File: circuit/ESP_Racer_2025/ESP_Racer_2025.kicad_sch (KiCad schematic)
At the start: 19 parts, among them IC1 XCL102D333CR-G, J1 Conn_LED_1, J2 Conn_LED_2, J3 Conn_Servo, U1 DRV8835DSST, U2 SFV12R-2STE1LF, U3 ESP32-C3-WROOM-02

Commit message: pcb fix
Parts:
- J1, J2: footprint JST_ZH_B2B-ZR_1x02_P1.50mm_Vertical:JST_ZH_B2B-ZR_1x02_P1.50mm_Vertical -> Molex:Molex_PicoBlade_53047-0210_1x02_P1.25mm_Vertical
- J3: footprint JST_ZH_B3B-ZR_1x03_P1.50mm_Vertical:JST_ZH_B3B-ZR_1x03_P1.50mm_Vertical -> Molex:Molex_PicoBlade_53047-0310_1x03_P1.25mm_Vertical
- R6: value 10k -> 20k
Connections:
- net +3.3V: now also U1.12 (VCC)
- net +BATT: now also U1.1 (VM)
- net AIN 1: now also U3.17 (GPIO1/ADC1_CH1/XTAL_N); no longer U3.16 (GPIO2/ADC1_CH2/FSPIQ)
- net GND: now also C2.2, C3.2
- net Servo_PWM: now also U3.5 (GPIO6/FSPICLK/MTCK); no longer U3.17 (GPIO1/ADC1_CH1/XTAL_N)
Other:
- note removed: "少しパターンを細長くして電流のピークを抑える"
- moved on the sheet: C2, C3

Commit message: add PIO
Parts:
- C5: value 0.1μF -> 0.1u
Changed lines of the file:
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@@
 			)
 		)
-		(property "Value" "0.1μF"
+		(property "Value" "0.1u"
 			(at 124.46 146.685 0)
 			(effects

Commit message: update pcb
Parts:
- C3: value 0.1u -> 10u
- R2, R3: value 330 -> 300
- R5: value 330 -> 1k
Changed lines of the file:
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@@
 			)
 		)
-		(property "Value" "330"
+		(property "Value" "300"
 			(at 245.11 89.154 90)
 			(effects
@@
 			)
 		)
-		(property "Value" "330"
+		(property "Value" "300"
 			(at 245.11 76.454 90)
 			(effects
@@
 			)
 		)
-		(property "Value" "0.1u"
+		(property "Value" "10u"
 			(at 118.11 80.0099 0)
 			(effects
@@
 			)
 		)
-		(property "Value" "330"
+		(property "Value" "1k"
 			(at 245.364 134.62 90)
 			(effects

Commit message: update firmware
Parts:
- added R7: 10k, Resistor_SMD:R_0603_1608Metric_Pad0.98x0.95mm_HandSolder, symbol Device:R
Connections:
- net +3.3V: now also R7.2; no longer J3.1 (Pin_1)
- net +BATT: now also J3.1 (Pin_1)
- net at U3.2 (EN): now also R7.1
- no-connect marks 10 -> 9
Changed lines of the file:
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@@
 	)
 	(junction
+		(at 184.15 76.2)
+		(diameter 0)
+		(color 0 0 0 0)
+	)
+	(junction
 		(at 93.98 80.01)
 		(diameter 0)
@@
 	)
 	(no_connect
-		(at 165.1 83.82)
-	)
-	(no_connect
 		(at 165.1 109.22)
 	)
@@
 	(wire
 		(pts
+			(xy 184.15 76.2) (xy 184.15 78.74)
+		)
+		(stroke
+			(width 0)
+			(type default)
+		)
+	)
+	(wire
+		(pts
 			(xy 120.65 137.16) (xy 120.65 140.97)
 		)
@@
 	(wire
 		(pts
+			(xy 184.15 73.66) (xy 184.15 76.2)
+		)
+		(stroke
+			(width 0)
+			(type default)
+		)
+	)
+	(wire
+		(pts
 			(xy 153.67 31.75) (xy 171.45 31.75)
 		)
@@
 	(wire
 		(pts
+			(xy 158.75 76.2) (xy 184.15 76.2)
+		)
+		(stroke
+			(width 0)
+			(type default)
+		)
+	)
+	(wire
+		(pts
 			(xy 96.52 82.55) (xy 96.52 87.63)
 		)
@@
 	(wire
 		(pts
+			(xy 158.75 83.82) (xy 165.1 83.82)
+		)
+		(stroke
+			(width 0)
+			(type default)
+		)
+	)
+	(wire
+		(pts
 			(xy 121.92 31.75) (xy 121.92 34.29)
 		)
@@
 	)
 	(symbol
+		(lib_id "Device:R")
+		(at 158.75 80.01 180)
+		(unit 1)
+		(exclude_from_sim no)
+		(in_bom yes)
+		(on_board yes)
+		(dnp no)
+		(property "Reference" "R7"
+			(at 154.686 80.01 90)
+			(effects
+				(font
+					(size 1.27 1.27)
+				)
+			)
+		)
+		(property "Value" "10k"
+			(at 156.464 80.01 90)
+			(effects
+				(font
+					(size 1.27 1.27)
+				)
+			)
+		)
+		(property "Footprint" "Resistor_SMD:R_0603_1608Metric_Pad0.98x0.95mm_HandSolder"
+			(at 160.528 80.01 90)
+			(effects
+				(font
+					(size 1.27 1.27)
+				)
+				(hide yes)
+			)
+		)
+		(property "Datasheet" "~"
+			(at 158.75 80.01 0)
+			(effects
+				(font
+					(size 1.27 1.27)
+				)
+				(hide yes)
+			)
+		)
+		(property "Description" "Resistor"
+			(at 158.75 80.01 0)
+			(effects
+				(font
+					(size 1.27 1.27)
+				)
+				(hide yes)
+			)
+		)
+		(pin "1"
+		)
+		(pin "2"
+		)
+		(instances
+			(project "ESP_Racer_2025"
+				(path "/5c50a387-df5f-414d-8825-9a6969b82251"
+					(reference "R7")
+					(unit 1)
+				)
+			)
+		)
+	)
+	(symbol
 		(lib_id "Device:C")
 		(at 130.81 38.1 0)
@@
 	)
 	(symbol
+		(lib_id "power:+BATT")
+		(at 245.11 102.87 0)
+		(unit 1)
+		(exclude_from_sim no)
+		(in_bom yes)
+		(on_board yes)
+		(dnp no)
+		(fields_autoplaced yes)
+		(property "Reference" "#PWR020"
+			(at 245.11 106.68 0)
+			(effects
+				(font
+					(size 1.27 1.27)
+				)
+				(hide yes)
+			)
+		)
+		(property "Value" "+BATT"
+			(at 245.11 97.79 0)
+			(effects
+				(font
+					(size 1.27 1.27)
+				)
+			)
+		)
+		(property "Footprint" ""
+			(at 245.11 102.87 0)
+			(effects
+				(font
+					(size 1.27 1.27)
+				)
+				(hide yes)
+			)
+		)
+		(property "Datasheet" ""
+			(at 245.11 102.87 0)
+			(effects
+				(font
+					(size 1.27 1.27)
+				)
+				(hide yes)
+			)
+		)
+		(property "Description" "Power symbol creates a global label with name \"+BATT\""
+			(at 245.11 102.87 0)
+			(effects
+				(font
+					(size 1.27 1.27)
+				)
+				(hide yes)
+			)
+		)
+		(pin "1"
+		)
+		(instances
+			(project "ESP_Racer_2025"
+				(path "/5c50a387-df5f-414d-8825-9a6969b82251"
+					(reference "#PWR020")
+					(unit 1)
+				)
+			)
+		)
+	)
+	(symbol
 		(lib_id "Connector:Conn_01x02_Socket")
 		(at 255.27 78.74 0)
@@
 	)
 	(symbol
-		(lib_id "power:+3.3V")
-		(at 245.11 102.87 0)
-		(unit 1)
-		(exclude_from_sim no)
-		(in_bom yes)
-		(on_board yes)
-		(dnp no)
-		(fields_autoplaced yes)
-		(property "Reference" "#PWR020"
-			(at 245.11 106.68 0)
-			(effects
-				(font
-					(size 1.27 1.27)
-				)
-				(hide yes)
-			)
-		)
-		(property "Value" "+3.3V"
-			(at 245.11 97.79 0)
-			(effects
-				(font
-					(size 1.27 1.27)
-				)
-			)
-		)
-		(property "Footprint" ""
-			(at 245.11 102.87 0)
-			(effects
-				(font
-					(size 1.27 1.27)
-				)
-				(hide yes)
-			)
-		)
-		(property "Datasheet" ""
-			(at 245.11 102.87 0)
-			(effects
-				(font
-					(size 1.27 1.27)
-				)
-				(hide yes)
-			)
-		)
-		(property "Description" "Power symbol creates a global label with name \"+3.3V\""
-			(at 245.11 102.87 0)
-			(effects
-				(font
-					(size 1.27 1.27)
-				)
-				(hide yes)
-			)
-		)
-		(pin "1"
-		)
-		(instances
-			(project "ESP_Racer_2025"
-				(path "/5c50a387-df5f-414d-8825-9a6969b82251"
-					(reference "#PWR020")
-					(unit 1)
-				)
-			)
-		)
-	)
-	(symbol
 		(lib_id "Device:C")
 		(at 124.46 78.74 0)
@@
 	(symbol
 		(lib_id "power:+3.3V")
-		(at 184.15 78.74 0)
+		(at 184.15 73.66 0)
 		(unit 1)
 		(exclude_from_sim no)
@@
 		(fields_autoplaced yes)
 		(property "Reference" "#PWR015"
-			(at 184.15 82.55 0)
+			(at 184.15 77.47 0)
 			(effects
 				(font
@@
 		)
 		(property "Value" "+3.3V"
-			(at 184.15 73.66 0)
+			(at 184.15 68.58 0)
 			(effects
 				(font
@@
 		)
 		(property "Footprint" ""
-			(at 184.15 78.74 0)
+			(at 184.15 73.66 0)
 			(effects
 				(font
@@
 		)
 		(property "Datasheet" ""
-			(at 184.15 78.74 0)
+			(at 184.15 73.66 0)
 			(effects
 				(font
@@
 		)
 		(property "Description" "Power symbol creates a global label with name \"+3.3V\""
-			(at 184.15 78.74 0)
+			(at 184.15 73.66 0)
 			(effects
 				(font

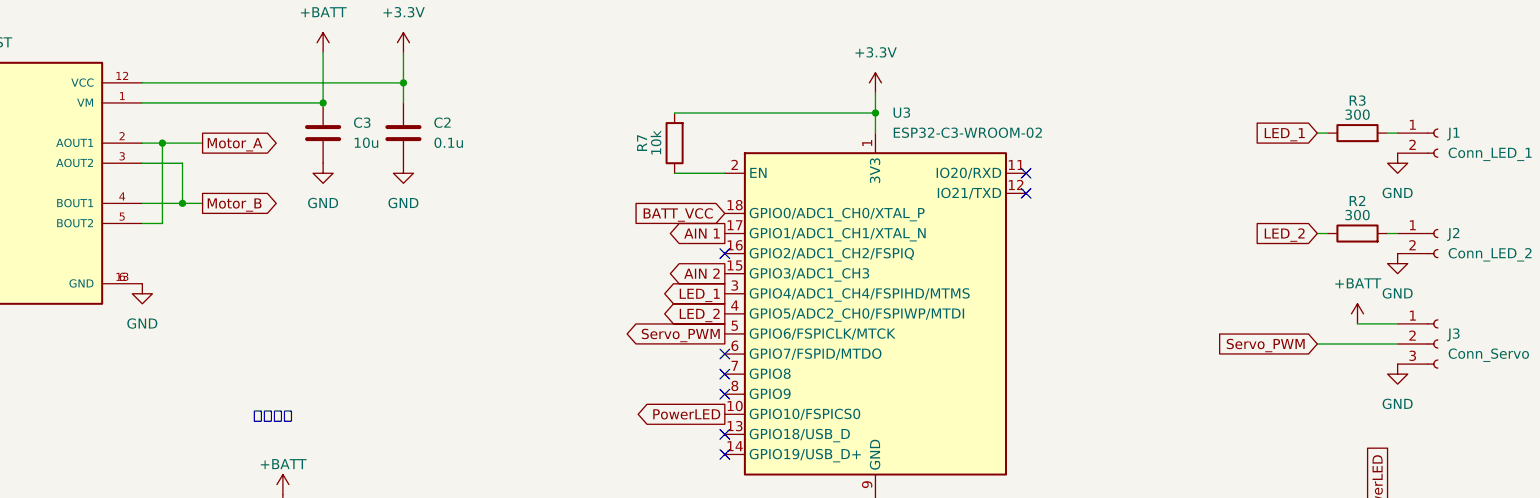
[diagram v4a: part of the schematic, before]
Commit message: fix hardware errors
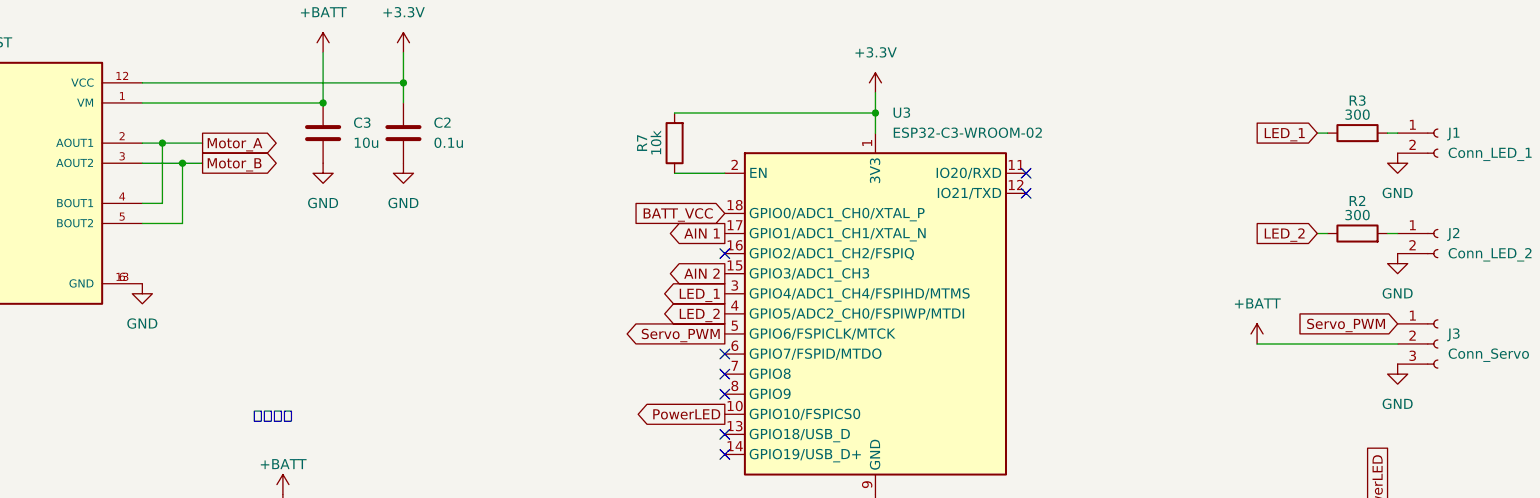
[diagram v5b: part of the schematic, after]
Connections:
- net +BATT: now also J3.2 (Pin_2); no longer J3.1 (Pin_1)
- net Motor_A: now also U1.4 (BOUT1); no longer U1.5 (BOUT2)
- net Motor_B: now also U1.5 (BOUT2); no longer U1.4 (BOUT1)
- net Servo_PWM: now also J3.1 (Pin_1); no longer J3.2 (Pin_2)

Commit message: fix pcb
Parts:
- added J4: Conn_USB, Original:Serial, symbol Connector:Conn_01x03_Socket
- added Q3: IRLML6402, IRLML6402:SOT23, symbol IRLML6402:IRLML6402
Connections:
- net +BATT: now also Q3.2; no longer U2.1, U2.2, U2.3
- net GND: now also J4.3 (Pin_3), Q3.1
- net USB_D-: now reaches U3.13 (GPIO18/USB_D)
- net USB_D-: now also J4.1 (Pin_1)
- net USB_D+: now reaches U3.14 (GPIO19/USB_D+)
- net USB_D+: now also J4.2 (Pin_2)
- new net: Q3.3, U2.1, U2.2, U2.3
- no-connect marks 9 -> 7
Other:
- note added: "逆接防止"

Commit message: pcb update
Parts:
- Q3: value IRLML6402 -> DMG3415U
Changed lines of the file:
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@@
 			)
 		)
-		(property "Value" "IRLML6402"
+		(property "Value" "DMG3415U"
 			(at 73.914 39.37 90)
 			(effects
